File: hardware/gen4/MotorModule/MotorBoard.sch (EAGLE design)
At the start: 67 parts, among them IC1 XMEGA16A4A, M1O1 TEST_PT, M1O2 TEST_PT, M1O3 TEST_PT

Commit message: motor board v2 done
things to do, address clearance and maybe change min trace width
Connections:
- removed net VREG: JP1.2
- net 3.3V: now also JP1.2
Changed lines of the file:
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@@
-</segment>
-</net>
-<net name="VREG" class="0">
-<segment>
-<pinref part="JP1" gate="G$1" pin="2"/>
-<wire x1="38.1" y1="73.66" x2="43.18" y2="73.66" width="0.1524" layer="91"/>
 </segment>
 </net>
@@
 <label x="20.32" y="177.8" size="1.778" layer="95"/>
 </segment>
-</net>
+<segment>
+<pinref part="JP1" gate="G$1" pin="2"/>
+<wire x1="38.1" y1="73.66" x2="43.18" y2="73.66" width="0.1524" layer="91"/>
+</segment>
+</net>

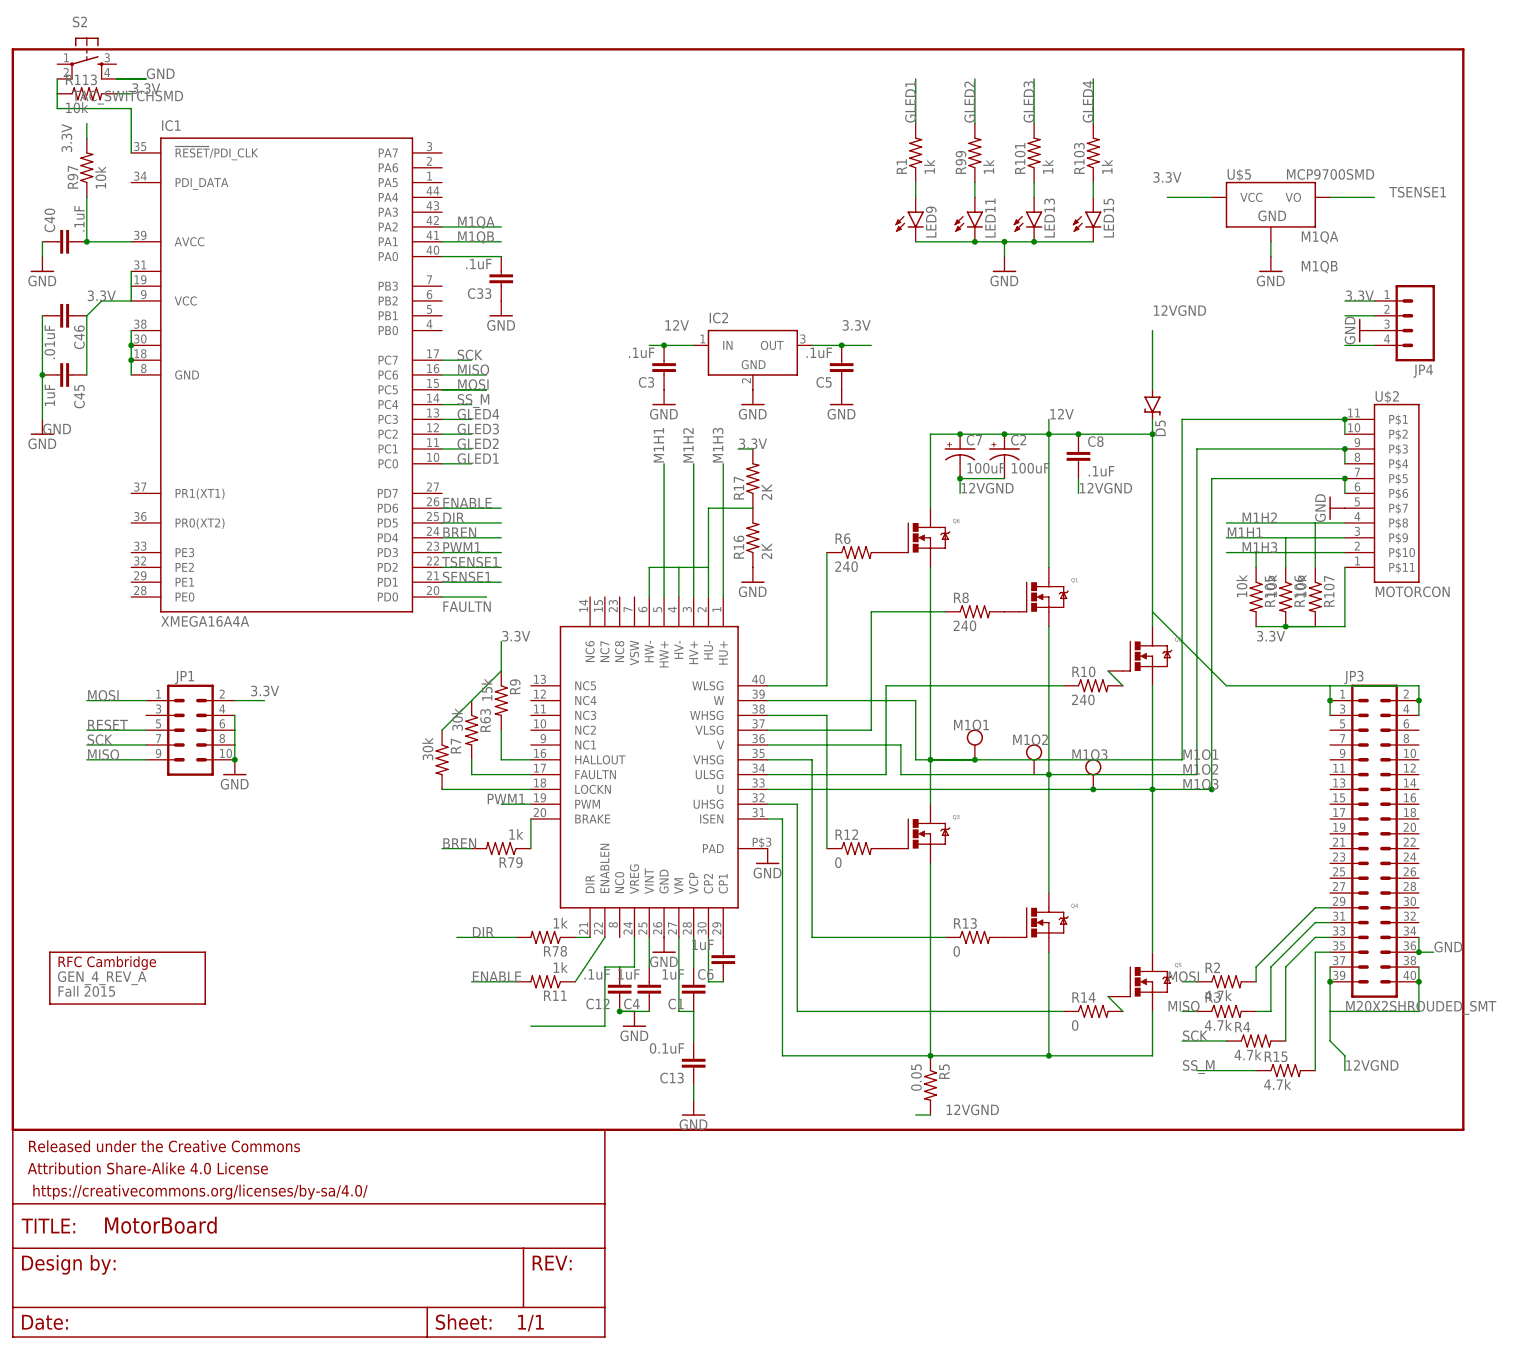
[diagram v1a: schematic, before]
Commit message: added new discharge circuit - spruced up for design review
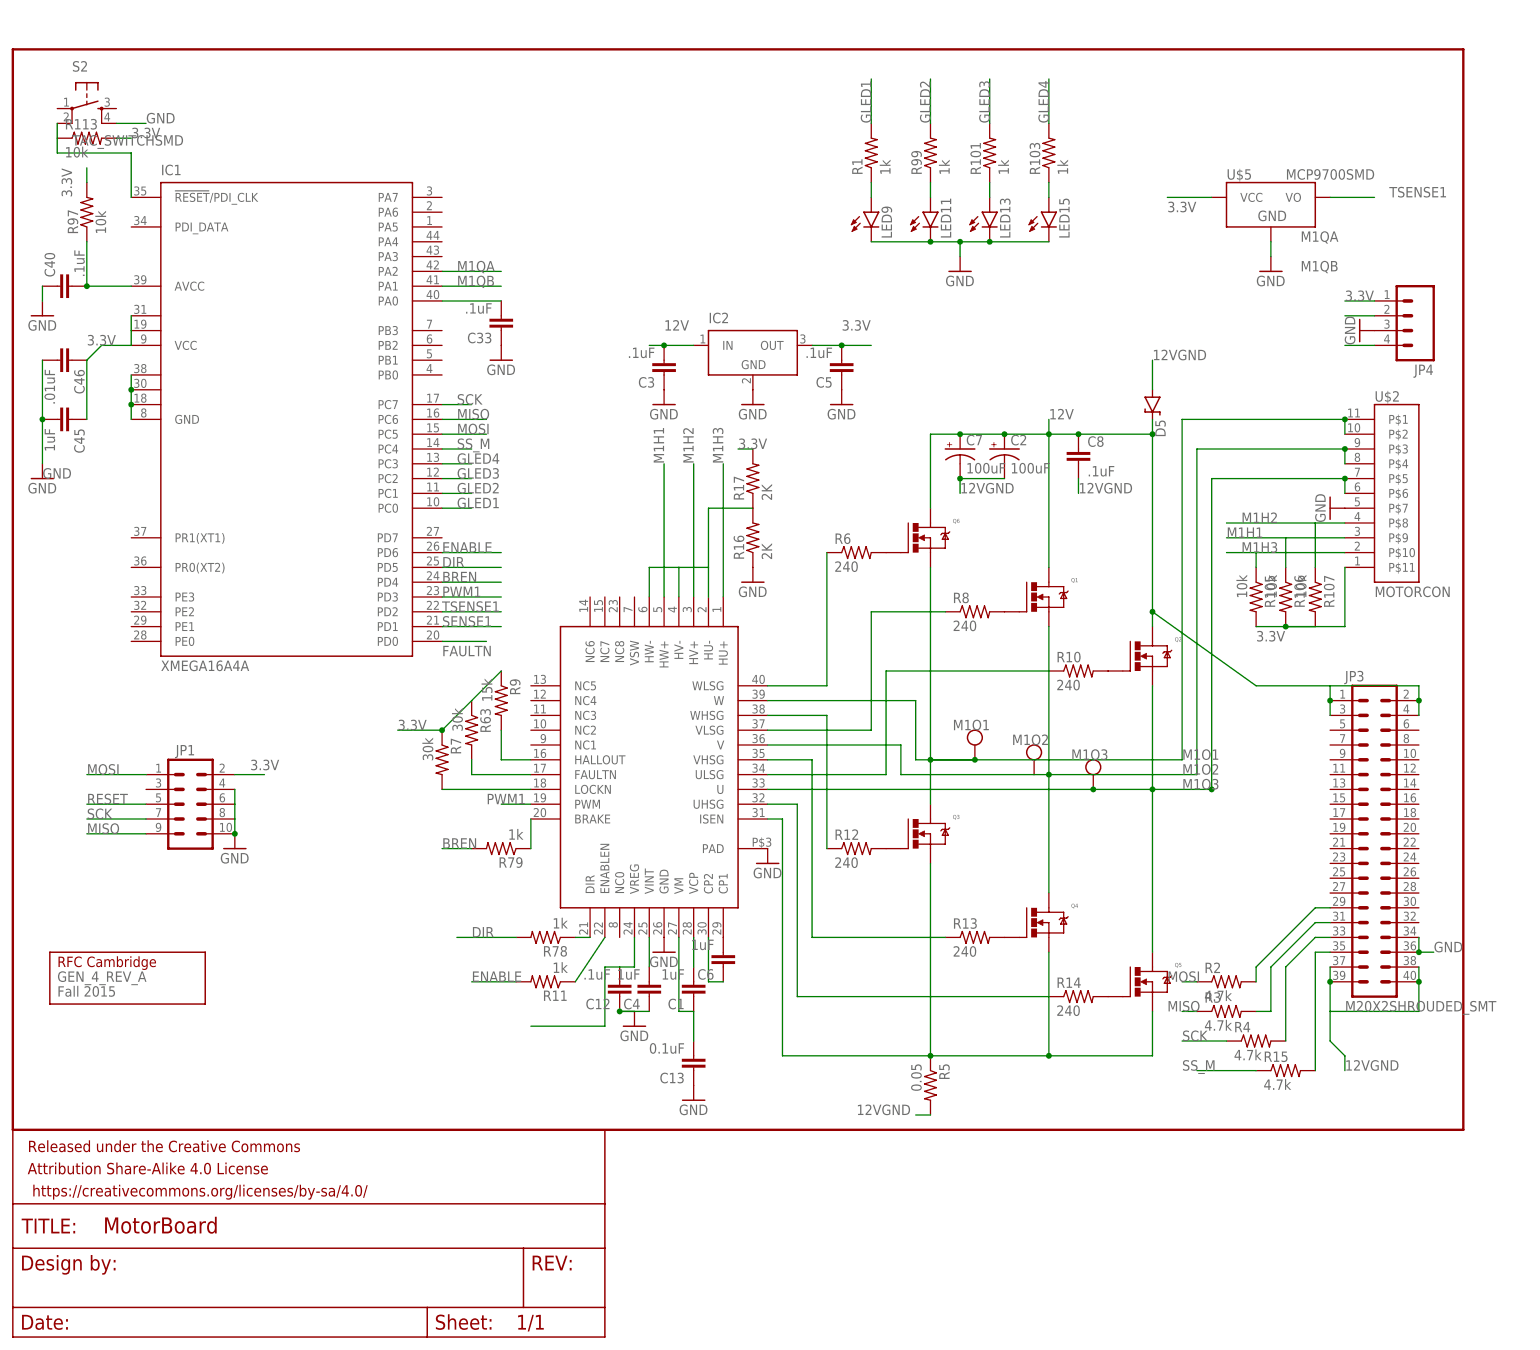
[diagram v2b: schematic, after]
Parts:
- R12, R13, R14: value 0 -> 240
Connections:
- net MISO: now also JP1.9
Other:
- moved on the sheet: C33, C40, C45, C46, IC1, JP1, LED11, LED13, LED15, LED9, R1, R10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

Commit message: motor board done
all connections done, size slightly larger
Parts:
- R12, R13, R14: value 240 -> 0
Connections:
- removed net N$33: JP3.34, JP3.36
- net GND: now also JP3.34, JP3.36
- net MISO: no longer JP1.9
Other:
- moved on the sheet: C33, C40, C45, C46, IC1, JP1, LED11, LED13, LED15, LED9, R1, R10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

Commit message: cleaned up a few things
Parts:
- R12, R13, R14: value 0 -> 240
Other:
- moved on the sheet: R10, R14
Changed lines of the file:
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@@
 <part name="R8" library="SparkFun-Resistors" deviceset="RESISTOR" device="0805-RES" value="240"/>
 <part name="R10" library="SparkFun-Resistors" deviceset="RESISTOR" device="0805-RES" value="240"/>
-<part name="R12" library="SparkFun-Resistors" deviceset="RESISTOR" device="0805-RES" value="0"/>
-<part name="R13" library="SparkFun-Resistors" deviceset="RESISTOR" device="0805-RES" value="0"/>
-<part name="R14" library="SparkFun-Resistors" deviceset="RESISTOR" device="0805-RES" value="0"/>
+<part name="R12" library="SparkFun-Resistors" deviceset="RESISTOR" device="0805-RES" value="240"/>
+<part name="R13" library="SparkFun-Resistors" deviceset="RESISTOR" device="0805-RES" value="240"/>
+<part name="R14" library="SparkFun-Resistors" deviceset="RESISTOR" device="0805-RES" value="240"/>
 <part name="R78" library="SparkFun-Resistors" deviceset="RESISTOR" device="0805-RES" value="1k"/>
 <part name="R79" library="SparkFun-Resistors" deviceset="RESISTOR" device="0805-RES" value="1k"/>
@@
 <instance part="R6" gate="G$1" x="144.78" y="99.06"/>
 <instance part="R8" gate="G$1" x="165.1" y="88.9"/>
-<instance part="R10" gate="G$1" x="185.42" y="76.2"/>
+<instance part="R10" gate="G$1" x="180.34" y="78.74"/>
 <instance part="R12" gate="G$1" x="144.78" y="48.26"/>
 <instance part="R13" gate="G$1" x="165.1" y="33.02"/>
-<instance part="R14" gate="G$1" x="185.42" y="20.32"/>
+<instance part="R14" gate="G$1" x="185.42" y="22.86"/>
 <instance part="R78" gate="G$1" x="91.44" y="33.02" rot="R180"/>
 <instance part="R79" gate="G$1" x="83.82" y="48.26" rot="R180"/>
@@
 <pinref part="Q2" gate="G$1" pin="P$3"/>
 <pinref part="R10" gate="G$1" pin="2"/>
-<wire x1="187.96" y1="78.74" x2="190.5" y2="76.2" width="0.1524" layer="91"/>
+<wire x1="187.96" y1="78.74" x2="185.42" y2="78.74" width="0.1524" layer="91"/>
 </segment>
 </net>
@@
 <pinref part="Q5" gate="G$1" pin="P$3"/>
 <pinref part="R14" gate="G$1" pin="2"/>
-<wire x1="187.96" y1="22.86" x2="190.5" y2="20.32" width="0.1524" layer="91"/>
+<wire x1="187.96" y1="22.86" x2="190.5" y2="22.86" width="0.1524" layer="91"/>
 </segment>
 </net>
@@
 <segment>
 <wire x1="129.54" y1="55.88" x2="134.62" y2="55.88" width="0.1524" layer="91"/>
-<wire x1="134.62" y1="55.88" x2="134.62" y2="20.32" width="0.1524" layer="91"/>
+<wire x1="134.62" y1="55.88" x2="134.62" y2="22.86" width="0.1524" layer="91"/>
 <pinref part="R14" gate="G$1" pin="1"/>
-<wire x1="134.62" y1="20.32" x2="180.34" y2="20.32" width="0.1524" layer="91"/>
+<wire x1="134.62" y1="22.86" x2="180.34" y2="22.86" width="0.1524" layer="91"/>
 <pinref part="U$1" gate="G$1" pin="UHSG"/>
 </segment>
@@
 <segment>
 <pinref part="R10" gate="G$1" pin="1"/>
-<wire x1="180.34" y1="76.2" x2="149.86" y2="76.2" width="0.1524" layer="91"/>
-<wire x1="149.86" y1="76.2" x2="149.86" y2="60.96" width="0.1524" layer="91"/>
+<wire x1="175.26" y1="78.74" x2="149.86" y2="78.74" width="0.1524" layer="91"/>
+<wire x1="149.86" y1="78.74" x2="149.86" y2="60.96" width="0.1524" layer="91"/>
 <wire x1="129.54" y1="60.96" x2="149.86" y2="60.96" width="0.1524" layer="91"/>
 <pinref part="U$1" gate="G$1" pin="ULSG"/>

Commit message: fixing motorboard
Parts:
- removed JP1: (no value), SparkFun-Connectors:M05X2SHD-NS
- removed U$2: MOTORCON, gen3:MOTORCON
- added JP2: (no value), pinhead:PINHD-2X3
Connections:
- new net DATA: IC1.PDI_DATA, JP2.1
- net 3.3V: now also JP2.2, JP3.23; no longer JP1.2, U$2.P$11
- net GND: now also JP2.6, JP3.15; no longer JP1.10, JP1.4, JP1.6, JP1.8, U$2.P$7
- net M1H1: now also JP3.19; no longer U$2.P$9
- net M1H2: now also JP3.17; no longer U$2.P$8
- net M1H3: now also JP3.21; no longer U$2.P$10
- net M1O1: now also JP3.10, JP3.9; no longer U$2.P$1, U$2.P$2
- net M1O2: now also JP3.11, JP3.12; no longer U$2.P$3, U$2.P$4
- net M1O3: now also JP3.13, JP3.14; no longer U$2.P$5, U$2.P$6
- net MOSI: no longer JP1.1
- net RESET: now also JP2.5; no longer JP1.5
- net SCK: no longer JP1.7
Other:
- moved on the sheet: R105, R106, R107

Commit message: more changes
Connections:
- new net 5V: C12.2, R17.2, R63.1, R7.1, R9.1, U$1.VREG
- net 3.3V: no longer C12.2, R17.2, R63.1, R7.1, R9.1, U$1.VREG
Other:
- note added: "5V"
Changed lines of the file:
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@@
 <text x="73.66" y="106.68" size="1.778" layer="95">ENABLE</text>
 <text x="78.74" y="33.02" size="1.778" layer="95">DIR</text>
+<text x="88.9" y="17.78" size="1.778" layer="95">5V</text>
+<text x="83.82" y="83.82" size="1.778" layer="95">5V</text>
+<text x="127" y="116.84" size="1.778" layer="95">5V</text>
 </plain>
 <instances>
@@
 <instance part="R11" gate="G$1" x="91.44" y="25.4" rot="R180"/>
 <instance part="R15" gate="G$1" x="218.44" y="10.16"/>
-<instance part="GND1" gate="1" x="38.1" y="60.96"/>
+<instance part="GND1" gate="1" x="40.64" y="66.04"/>
 <instance part="IC2" gate="G$1" x="127" y="132.08"/>
 <instance part="GND4" gate="1" x="127" y="124.46"/>
@@
 </segment>
 <segment>
-<wire x1="33.02" y1="68.58" x2="38.1" y2="63.5" width="0.1524" layer="91"/>
+<wire x1="33.02" y1="68.58" x2="40.64" y2="68.58" width="0.1524" layer="91"/>
 <pinref part="GND1" gate="1" pin="GND"/>
 <pinref part="JP2" gate="A" pin="6"/>
@@
 <label x="142.24" y="137.16" size="1.778" layer="95"/>
 <label x="12.7" y="142.24" size="1.778" layer="95"/>
-<label x="124.46" y="116.84" size="1.778" layer="95"/>
 <label x="228.6" y="142.24" size="1.778" layer="95"/>
 </segment>
@@
 </segment>
 <segment>
-<wire x1="88.9" y1="17.78" x2="101.6" y2="17.78" width="0.1524" layer="91"/>
-<wire x1="101.6" y1="17.78" x2="101.6" y2="27.94" width="0.1524" layer="91"/>
-<pinref part="C12" gate="G$1" pin="2"/>
-<wire x1="106.68" y1="33.02" x2="106.68" y2="27.94" width="0.1524" layer="91"/>
-<wire x1="106.68" y1="27.94" x2="104.14" y2="27.94" width="0.1524" layer="91"/>
-<wire x1="101.6" y1="27.94" x2="104.14" y2="27.94" width="0.1524" layer="91"/>
-<pinref part="U$1" gate="G$1" pin="VREG"/>
-</segment>
-<segment>
 <pinref part="U$5" gate="G$1" pin="VCC"/>
 <wire x1="205.74" y1="160.02" x2="198.12" y2="160.02" width="0.1524" layer="91"/>
 <label x="195.58" y="162.56" size="1.778" layer="95"/>
-<label x="83.82" y="83.82" size="1.778" layer="95"/>
-</segment>
-<segment>
-<pinref part="R17" gate="G$1" pin="2"/>
-<wire x1="127" y1="116.84" x2="124.46" y2="116.84" width="0.1524" layer="91"/>
 </segment>
 <segment>
@@
 </segment>
 <segment>
-<pinref part="R7" gate="G$1" pin="1"/>
-<pinref part="R63" gate="G$1" pin="1"/>
-<wire x1="73.66" y1="68.58" x2="78.74" y2="73.66" width="0.1524" layer="91"/>
-<pinref part="R9" gate="G$1" pin="1"/>
-<wire x1="78.74" y1="73.66" x2="83.82" y2="78.74" width="0.1524" layer="91"/>
-<wire x1="83.82" y1="78.74" x2="83.82" y2="83.82" width="0.1524" layer="91"/>
-</segment>
-<segment>
 <pinref part="R113" gate="G$1" pin="2"/>
 <wire x1="17.78" y1="177.8" x2="20.32" y2="177.8" width="0.1524" layer="91"/>
@@
 </segment>
 </net>
+<net name="5V" class="0">
+<segment>
+<wire x1="88.9" y1="17.78" x2="101.6" y2="17.78" width="0.1524" layer="91"/>
+<wire x1="101.6" y1="17.78" x2="101.6" y2="27.94" width="0.1524" layer="91"/>
+<pinref part="C12" gate="G$1" pin="2"/>
+<wire x1="106.68" y1="33.02" x2="106.68" y2="27.94" width="0.1524" layer="91"/>
+<wire x1="106.68" y1="27.94" x2="104.14" y2="27.94" width="0.1524" layer="91"/>
+<wire x1="101.6" y1="27.94" x2="104.14" y2="27.94" width="0.1524" layer="91"/>
+<pinref part="U$1" gate="G$1" pin="VREG"/>
+</segment>
+<segment>
+<pinref part="R7" gate="G$1" pin="1"/>
+<pinref part="R63" gate="G$1" pin="1"/>
+<wire x1="73.66" y1="68.58" x2="73.66" y2="73.66" width="0.1524" layer="91"/>
+<wire x1="73.66" y1="73.66" x2="78.74" y2="73.66" width="0.1524" layer="91"/>
+<pinref part="R9" gate="G$1" pin="1"/>
+<wire x1="78.74" y1="73.66" x2="78.74" y2="78.74" width="0.1524" layer="91"/>
+<wire x1="78.74" y1="78.74" x2="83.82" y2="78.74" width="0.1524" layer="91"/>
+<junction x="78.74" y="73.66"/>
+<wire x1="83.82" y1="78.74" x2="83.82" y2="83.82" width="0.1524" layer="91"/>
+<junction x="83.82" y="78.74"/>
+</segment>
+<segment>
+<pinref part="R17" gate="G$1" pin="2"/>
+<wire x1="127" y1="116.84" x2="129.54" y2="116.84" width="0.1524" layer="91"/>
+</segment>
+</net>
